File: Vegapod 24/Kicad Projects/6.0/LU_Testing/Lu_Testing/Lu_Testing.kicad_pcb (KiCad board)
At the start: 2 copper layers, 153.4 x 87.4 mm, 101 parts, among them J1 DC Link, J2 OUT, J3 17V-35V IN, Q1 Q_NMOS_GDS, Q2 Q_NMOS_GDS, Q3 Q_PMOS_GSD, Q4 Q_PMOS_GSD, Q5 Q_PMOS_GSD, U1 LM7815_TO220, U2 KA78M05_TO252, U3 IR2110, U4 B0505S-1WR3, U5 LM324, U6 6N137, U7 6N137, U8 6N137

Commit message: LU PCB
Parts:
- R37, R38: moved to B.Cu
- moved R37 68.0 mm to (132.6, 88.8), turned to 180 degrees
- moved R38 58.6 mm to (132.6, 86.7), turned to 180 degrees
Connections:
- C32 pad 2: Net-(U5-Pad6) -> Net-(C32-Pad2)
- R37 pad 1: Net-(U5-Pad6) -> Net-(C32-Pad2)
- R38 pad 1: Net-(U5-Pad5) -> Net-(R38-Pad1)
- U5 pad 10: unconnected-(U5-Pad10) -> Net-(R38-Pad1)
- U5 pad 5: Net-(U5-Pad5) -> unconnected-(U5-Pad5)
- U5 pad 6: Net-(U5-Pad6) -> unconnected-(U5-Pad6)
- U5 pad 9: unconnected-(U5-Pad9) -> Net-(C32-Pad2)
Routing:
- net Net-(R38-Pad1): track 0.00 -> 6.69 mm
- net Net-(C32-Pad2): track 0.00 -> 5.31 mm
- net DC Link+: track 112.9 -> 111.1 mm
- net DC Link-: track 246.1 -> 245.4 mm

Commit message: Power side complete lu
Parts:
- added C33: 100n, Capacitor_SMD:C_0805_2012Metric_Pad1.18x1.45mm_HandSolder, B.Cu at (103.0, 68.7)
- added C34: 100n, Capacitor_SMD:C_0805_2012Metric_Pad1.18x1.45mm_HandSolder, B.Cu at (103.0, 39.9)
- added C35: 100n, Capacitor_SMD:C_0805_2012Metric_Pad1.18x1.45mm_HandSolder, B.Cu at (103.0, 28.4)
- added C36: 10u, Capacitor_SMD:C_1206_3216Metric_Pad1.33x1.80mm_HandSolder, B.Cu at (109.9, 46.1)
- added C37: 100n, Capacitor_SMD:C_0805_2012Metric_Pad1.18x1.45mm_HandSolder, B.Cu at (107.4, 46.7)
- added C38: 100n, Capacitor_SMD:C_0805_2012Metric_Pad1.18x1.45mm_HandSolder, F.Cu at (93.3, 46.1)
- added C39: 10u, Capacitor_SMD:C_1206_3216Metric_Pad1.33x1.80mm_HandSolder, F.Cu at (91.1, 46.0)
- added U10: ADUM4195-1BRIZ, ADUM4195-1:RI-8-1_ADI, F.Cu at (101.2, 46.1)
- added U9: 6N137, Package_DIP:DIP-8_W7.62mm, F.Cu at (105.3, 58.7)
- C32, Q3, Q4, Q5: moved to B.Cu
- R30: renamed from R39; moved to B.Cu
- R32: renamed from R40; moved to B.Cu
- R35: renamed from R31; moved to B.Cu
- R37: renamed from R32; moved to B.Cu
- R39: renamed from R33; moved to B.Cu
- moved R32 86.5 mm to (134.6, 100.3)
- moved R30 76.1 mm to (138.4, 100.3)
- moved Q4 75.6 mm to (109.5, 28.8), turned to -90 degrees
- moved Q5 71.8 mm to (109.0, 39.6), turned to -90 degrees
- moved R38 68.9 mm to (108.0, 29.2), turned to -90 degrees
- moved U7 63.6 mm to (97.7, 22.2)
- moved Q3 56.6 mm to (108.5, 68.5), turned to -90 degrees
- moved R39 54.6 mm to (103.0, 35.2), turned to -90 degrees
- moved R40 51.0 mm to (107.6, 40.8), turned to -90 degrees
- moved C32 50.8 mm to (107.6, 71.9)
- moved R36 46.8 mm to (107.6, 69.5), turned to -90 degrees
- moved R35 42.6 mm to (103.1, 64.5), turned to -90 degrees
- moved R37 42.3 mm to (103.0, 23.7), turned to -90 degrees
- moved U6 40.7 mm to (97.7, 62.1)
- moved U8 39.5 mm to (97.7, 33.5)
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- renumbered C11 to C1, C20 to C10, C5 to C11, C10 to C12, C8 to C13, C13 to C14, C17 to C15, C21 to C16, C6 to C17, C24 to C18, C14 to C19, C12 to C2, C1 to C20, C25 to C21, C2 to C23, C3 to C24, C23 to C25, C31 to C26, C26 to C27, C27 to C28, C28 to C29, C18 to C3, C29 to C30, C30 to C31, C9 to C5, C15 to C6, C19 to C7, C7 to C8, C16 to C9, D5 to D1, D6 to D2, D1 to D3, D8 to D4, D2 to D5, D4 to D6, D3 to D7, D7 to D8, J3 to J2, J2 to J3, R10 to R1, R20 to R10, R4 to R11, R26 to R12, R21 to R13, R28 to R14, R29 to R15, R30 to R16, R23 to R17, R1 to R18, R2 to R19, R13 to R2, R5 to R20, R6 to R21, R7 to R22, R8 to R23, R9 to R24, R12 to R25, R15 to R26, R18 to R27, R27 to R28, R24 to R29, R16 to R3, R25 to R31, R38 to R33, R37 to R34, R34 to R36, R35 to R38, R19 to R4, R36 to R40, R22 to R5, R11 to R6, R14 to R7, R17 to R8, R3 to R9, U2 to U1, U1 to U2, U4 to U3, U3 to U4
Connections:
- U5 pad 8: unconnected-(U5-Pad8) -> CO
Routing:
- net +5V: track 70.8 -> 187.5 mm, vias 5 -> 9
- net A0: track 0.00 -> 84.0 mm, vias 0 -> 5
- net CO: track 0.00 -> 57.7 mm, vias 0 -> 2
- net HIN: track 0.00 -> 51.7 mm, vias 0 -> 2
- net LIN: track 0.00 -> 45.1 mm, vias 0 -> 3
- net Net-(C32-Pad2): track 5.31 -> 45.3 mm
- net DC Link-: track 245.4 -> 258.4 mm, vias 4 -> 8
- net Net-(Q4-Pad1): track 0.00 -> 6.99 mm
- net Net-(C38-Pad2): track 0.00 -> 6.91 mm
- net Net-(Q5-Pad1): track 0.00 -> 6.14 mm
- net Net-(C38-Pad1): track 0.00 -> 5.64 mm
- net Net-(Q3-Pad1): track 0.00 -> 5.21 mm
- net Net-(Q3-Pad3): track 0.00 -> 4.59 mm, vias 0 -> 1
- net Net-(R12-Pad1): track 7.57 -> 10.7 mm
- net Net-(R33-Pad1): track 6.69 -> 7.77 mm
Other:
- board size 153.4 x 87.4 mm -> 169.3 x 87.4 mm

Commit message: LU testing board
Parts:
- added C35: 47n, Capacitor_SMD:C_0805_2012Metric_Pad1.18x1.45mm_HandSolder, F.Cu at (100.7, 90.7)
- added R39: 220, Resistor_SMD:R_0805_2012Metric_Pad1.20x1.40mm_HandSolder, F.Cu at (100.7, 93.7)
- added U9: STM32G474RET6, STM32G4:QFP50P1200X1200X160-64N, F.Cu at (90.6, 95.5)
- renumbered C35 to C36, C36 to C37, C37 to C38, C38 to C39, C39 to C40, R39 to R40, R40 to R41, U9 to U10, U10 to U11
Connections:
- C39 pad 1: Net-(C38-Pad1) -> +5VD
- C39 pad 2: Net-(C38-Pad2) -> GNDD
- C40 pad 1: Net-(C38-Pad1) -> +5VD
- C40 pad 2: Net-(C38-Pad2) -> GNDD
- U10 pad 5: unconnected-(U9-Pad5) -> GNDD
- U10 pad 6: unconnected-(U9-Pad6) -> DFB
- U10 pad 7: unconnected-(U9-Pad7) -> +5VD
- U10 pad 8: unconnected-(U9-Pad8) -> +5VD
- U11 pad 5: Net-(C38-Pad2) -> GNDD
- U11 pad 6: Net-(C38-Pad2) -> GNDD
- U11 pad 7: unconnected-(U10-Pad7) -> DA0
- U11 pad 8: Net-(C38-Pad1) -> +5VD
- U6 pad 2: unconnected-(U6-Pad2) -> DPWMADJ
- U6 pad 3: unconnected-(U6-Pad3) -> GNDD
- U7 pad 2: unconnected-(U7-Pad2) -> DHIN
- U7 pad 3: unconnected-(U7-Pad3) -> GNDD
- U8 pad 2: unconnected-(U8-Pad2) -> DLIN
- U8 pad 3: unconnected-(U8-Pad3) -> GNDD
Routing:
- net Net-(C38-Pad2): track 6.91 -> 0.00 mm
- net GNDD: track 0.00 -> 6.91 mm
- net Net-(C38-Pad1): track 5.64 -> 0.00 mm
- net +5VD: track 0.00 -> 5.64 mm
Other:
- board size 169.3 x 87.4 mm -> 175.9 x 87.4 mm

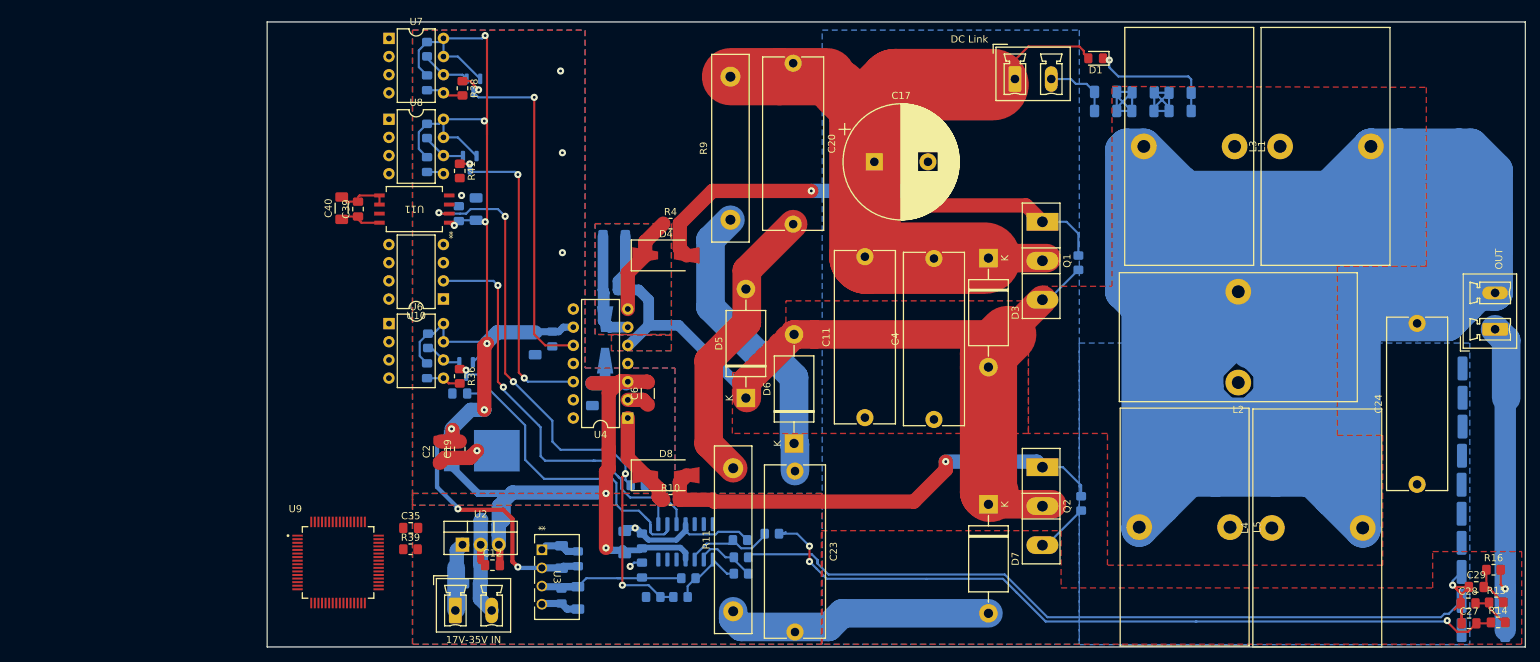
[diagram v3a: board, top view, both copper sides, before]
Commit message: UART and stlink missing lu board
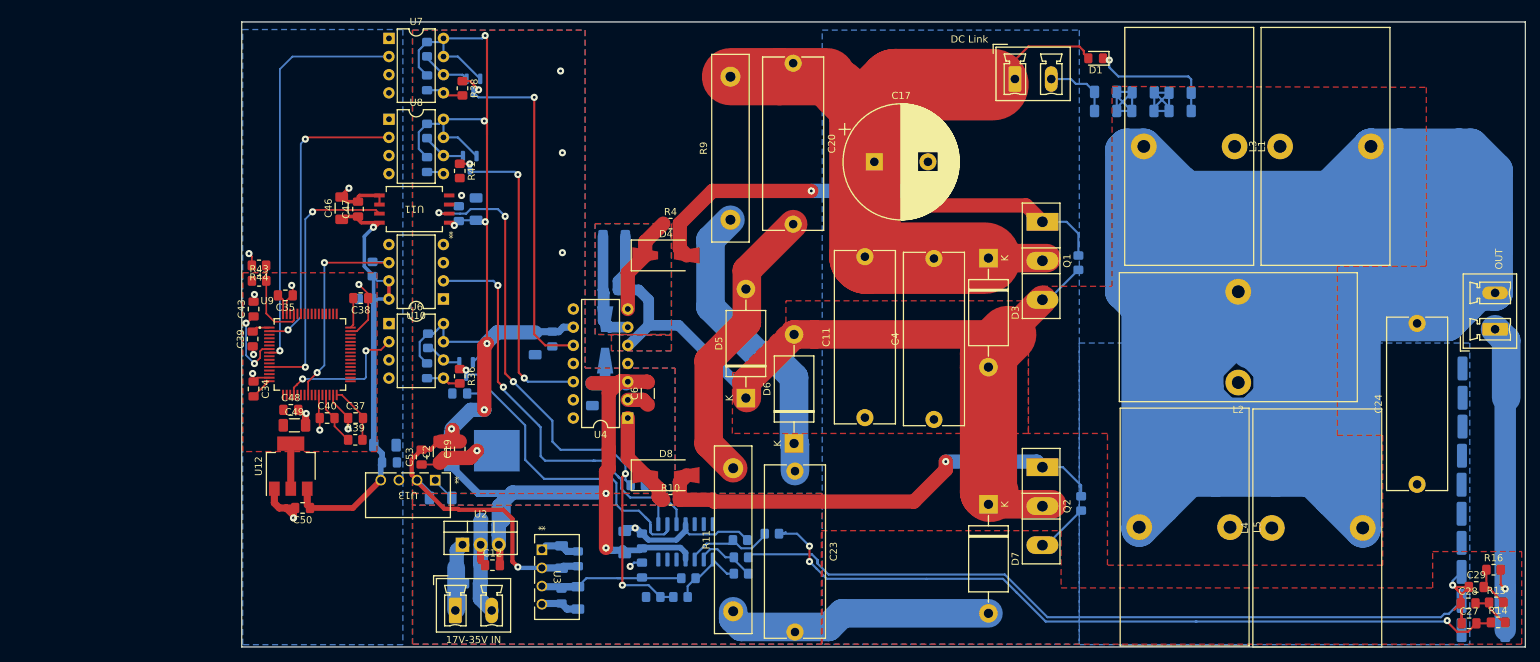
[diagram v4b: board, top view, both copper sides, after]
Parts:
- added C34: 100n, Capacitor_SMD:C_0805_2012Metric_Pad1.18x1.45mm_HandSolder, F.Cu at (78.7, 71.2)
- added C35: 100n, Capacitor_SMD:C_0805_2012Metric_Pad1.18x1.45mm_HandSolder, F.Cu at (83.2, 58.2)
- added C37: 100n, Capacitor_SMD:C_0805_2012Metric_Pad1.18x1.45mm_HandSolder, F.Cu at (93.0, 75.3)
- added C38: 100n, Capacitor_SMD:C_0805_2012Metric_Pad1.18x1.45mm_HandSolder, F.Cu at (93.7, 58.5)
- added C39: 100n, Capacitor_SMD:C_0805_2012Metric_Pad1.18x1.45mm_HandSolder, F.Cu at (78.6, 64.3)
- added C42: 100n, Capacitor_SMD:C_0805_2012Metric_Pad1.18x1.45mm_HandSolder, B.Cu at (94.5, 58.7)
- added C43: 100n, Capacitor_SMD:C_0805_2012Metric_Pad1.18x1.45mm_HandSolder, F.Cu at (78.7, 60.1)
- added C48: 100n, Capacitor_SMD:C_0805_2012Metric_Pad1.18x1.45mm_HandSolder, F.Cu at (83.9, 74.2)
- added C49: 10u, Capacitor_SMD:C_1206_3216Metric_Pad1.33x1.80mm_HandSolder, F.Cu at (84.5, 76.3)
- added C50: 100n, Capacitor_SMD:C_0805_2012Metric_Pad1.18x1.45mm_HandSolder, F.Cu at (85.6, 87.9)
- added C51: 100n, Capacitor_SMD:C_0805_2012Metric_Pad1.18x1.45mm_HandSolder, B.Cu at (97.7, 81.5)
- added C52: 10u, Capacitor_SMD:C_1206_3216Metric_Pad1.33x1.80mm_HandSolder, B.Cu at (97.1, 79.1)
- added C53: 100n, Capacitor_SMD:C_0805_2012Metric_Pad1.18x1.45mm_HandSolder, F.Cu at (102.2, 80.8)
- added C54: 10u, Capacitor_SMD:C_1206_3216Metric_Pad1.33x1.80mm_HandSolder, B.Cu at (104.9, 86.5)
- added R42: 470, Resistor_SMD:R_0805_2012Metric_Pad1.20x1.40mm_HandSolder, B.Cu at (95.4, 54.5)
- added R43: Open Circuit, Resistor_SMD:R_0805_2012Metric_Pad1.20x1.40mm_HandSolder, F.Cu at (79.5, 56.1)
- added R44: Short out, Resistor_SMD:R_0805_2012Metric_Pad1.20x1.40mm_HandSolder, F.Cu at (79.5, 54.0)
- added U12: AMS1117-3.3, Package_TO_SOT_SMD:SOT-223-3_TabPin2, F.Cu at (83.9, 82.0)
- added U13: B0505S-1WR3, B0505S-1WR3:B0505S_MNS, F.Cu at (104.1, 84.0)
- C40: renamed from C35; value 47n -> 100n
- R39: value 220 -> 10
- moved U9 29.3 mm to (86.6, 66.4)
- moved C40 19.3 mm to (89.0, 75.3)
- moved R39 17.1 mm to (93.0, 78.4)
- renumbered C34 to C36, C36 to C41, C38 to C44, C37 to C45, C40 to C46, C39 to C47
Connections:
- U9 pad 61: unconnected-(U9-Pad61) -> Net-(U9-Pad61)
- U9 pad 7: unconnected-(U9-Pad7) -> Net-(U9-Pad7)
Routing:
- net +5VD: track 5.64 -> 65.3 mm, vias 0 -> 1
- net DHIN: track 0.00 -> 56.9 mm, vias 0 -> 1
- net GNDD: track 6.91 -> 49.6 mm, vias 0 -> 11
- net DLIN: track 0.00 -> 42.2 mm, vias 0 -> 2
- net DA0: track 0.00 -> 36.8 mm, vias 0 -> 2
- net DFB: track 0.00 -> 30.8 mm, vias 0 -> 2
- net +3.3V: track 0.00 -> 27.2 mm
- net DPWMADJ: track 0.00 -> 19.2 mm, vias 0 -> 2
- net Net-(U9-Pad61): track 0.00 -> 12.1 mm
- net Net-(U9-Pad7): track 0.00 -> 11.0 mm, vias 0 -> 2
- net +5V: track 187.5 -> 195.6 mm, vias 9 -> 8
- net Net-(C40-Pad2): track 0.00 -> 7.55 mm
- net DC Link-: track 258.4 -> 264.5 mm
- added copper zone on F.Cu, net +3.3V
- added copper zone on B.Cu, net GNDD
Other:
- board size 175.9 x 87.4 mm -> 179.5 x 87.4 mm

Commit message: LU Board Semi Final
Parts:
- added C43: 100n, Capacitor_SMD:C_0805_2012Metric_Pad1.18x1.45mm_HandSolder, F.Cu at (79.1, 90.7)
- added C49: 10u, Capacitor_SMD:C_1206_3216Metric_Pad1.33x1.80mm_HandSolder, B.Cu at (86.7, 103.0)
- added C50: 100n, Capacitor_SMD:C_0805_2012Metric_Pad1.18x1.45mm_HandSolder, B.Cu at (90.6, 100.3)
- added J4: Conn_01x07_Male, Connector_PinHeader_2.54mm:PinHeader_1x07_P2.54mm_Vertical_SMD_Pin1Right, F.Cu at (80.6, 30.0)
- added J5: Conn_01x04_Male, Connector_PinHeader_2.54mm:PinHeader_1x04_P2.54mm_Vertical, F.Cu at (79.2, 49.4)
- added J6: Conn_01x04_Male, Connector_PinHeader_2.54mm:PinHeader_1x04_P2.54mm_Vertical, F.Cu at (83.3, 105.7)
- added R44: 470, Resistor_SMD:R_0805_2012Metric_Pad1.20x1.40mm_HandSolder, F.Cu at (82.9, 90.7)
- added R45: 470, Resistor_SMD:R_0805_2012Metric_Pad1.20x1.40mm_HandSolder, B.Cu at (79.5, 100.2)
- added R47: 470, Resistor_SMD:R_0805_2012Metric_Pad1.20x1.40mm_HandSolder, B.Cu at (83.4, 100.2)
- added R48: 470, Resistor_SMD:R_0805_2012Metric_Pad1.20x1.40mm_HandSolder, F.Cu at (94.2, 90.7)
- added R49: 470, Resistor_SMD:R_0805_2012Metric_Pad1.20x1.40mm_HandSolder, B.Cu at (94.5, 100.5)
- added R50: 470, Resistor_SMD:R_0805_2012Metric_Pad1.20x1.40mm_HandSolder, F.Cu at (98.0, 90.7)
- added U11: 6N137, Package_SO:SSO-8_6.7x9.8mm_P2.54mm_Clearance8mm, F.Cu at (82.4, 97.8)
- added U13: 6N137, Package_SO:SSO-8_6.7x9.8mm_P2.54mm_Clearance8mm, F.Cu at (93.1, 97.8)
- moved C53 2.54 mm to (88.1, 88.0)
- moved U14 2.54 mm to (86.5, 82.2)
- renumbered C43 to C44, C44 to C45, C45 to C46, C46 to C47, C47 to C48, C48 to C51, C49 to C52, C50 to C53, C51 to C54, C52 to C55, C53 to C56, C54 to C57, R44 to R46, U11 to U12, U12 to U14, U13 to U15
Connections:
- U9 pad 22: unconnected-(U9-Pad22) -> TXD
- U9 pad 23: unconnected-(U9-Pad23) -> RXD
- U9 pad 49: unconnected-(U9-Pad49) -> SWDIO
- U9 pad 50: unconnected-(U9-Pad50) -> SWCLK
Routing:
- net +5VD: track 65.3 -> 124.7 mm, vias 1 -> 2
- net DPWMADJ: track 19.2 -> 69.8 mm, vias 2 -> 3
- net DFB: track 30.8 -> 64.5 mm, vias 2 -> 3
- net TXD: track 0.00 -> 31.2 mm, vias 0 -> 2
- net DA0: track 36.8 -> 65.2 mm, vias 2 -> 3
- net SWCLK: track 0.00 -> 26.6 mm, vias 0 -> 2
- net RXD: track 0.00 -> 24.3 mm, vias 0 -> 2
- net SWDIO: track 0.00 -> 24.2 mm, vias 0 -> 2
- net GNDD: track 49.6 -> 70.8 mm, vias 11 -> 22
- net 5VCOMM: track 0.00 -> 15.1 mm, vias 0 -> 2
- net TXCOMM: track 0.00 -> 8.41 mm, vias 0 -> 1
- net DLIN: track 42.2 -> 50.3 mm
- net DHIN: track 56.9 -> 61.9 mm, vias 1 -> 3
- net Net-(R45-Pad1): track 0.00 -> 4.67 mm, vias 0 -> 1
- net Net-(R48-Pad2): track 0.00 -> 4.52 mm
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- added copper zone on F.Cu, net +5VD
- added copper zone on F.Cu, net 5VCOMM
- added copper zone on B.Cu, net GNDCOMM
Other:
- board text added: "3V3"
- board text added: "5V"
- board text added: "GND"
- board text added: "RX"
- board text added: "SWCLK"
- board text added: "SWDIO"
- board text added: "TX"
